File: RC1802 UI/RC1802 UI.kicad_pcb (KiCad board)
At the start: 2 copper layers, 99.1 x 80 mm, 47 parts, among them J1 Mount, J2 Mount, J3 Mount, J4 Mount, J6 CONN_02X20, SW1 CLEAR, SW10 IN5, SW11 IN6, SW12 IN7, SW2 IN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

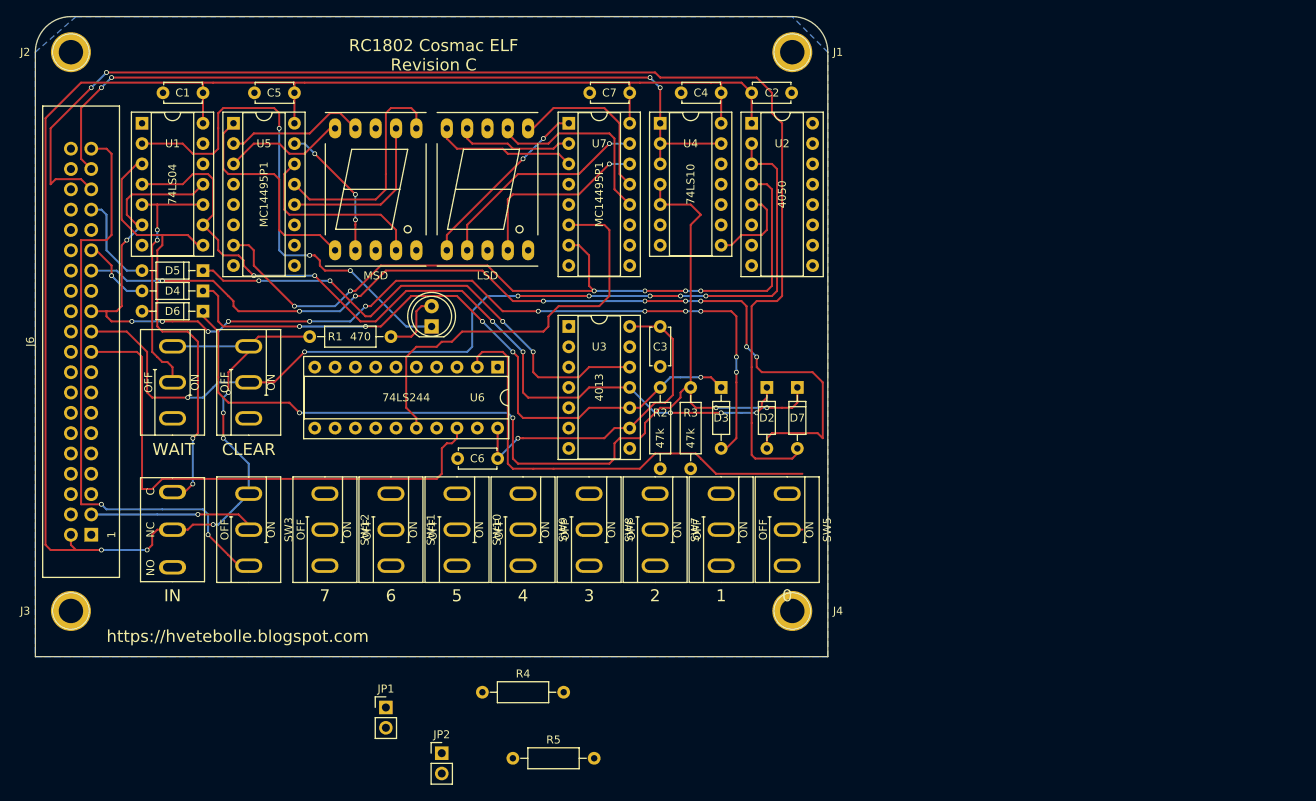
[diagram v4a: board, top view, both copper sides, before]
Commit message: Use proper switch names to ease use
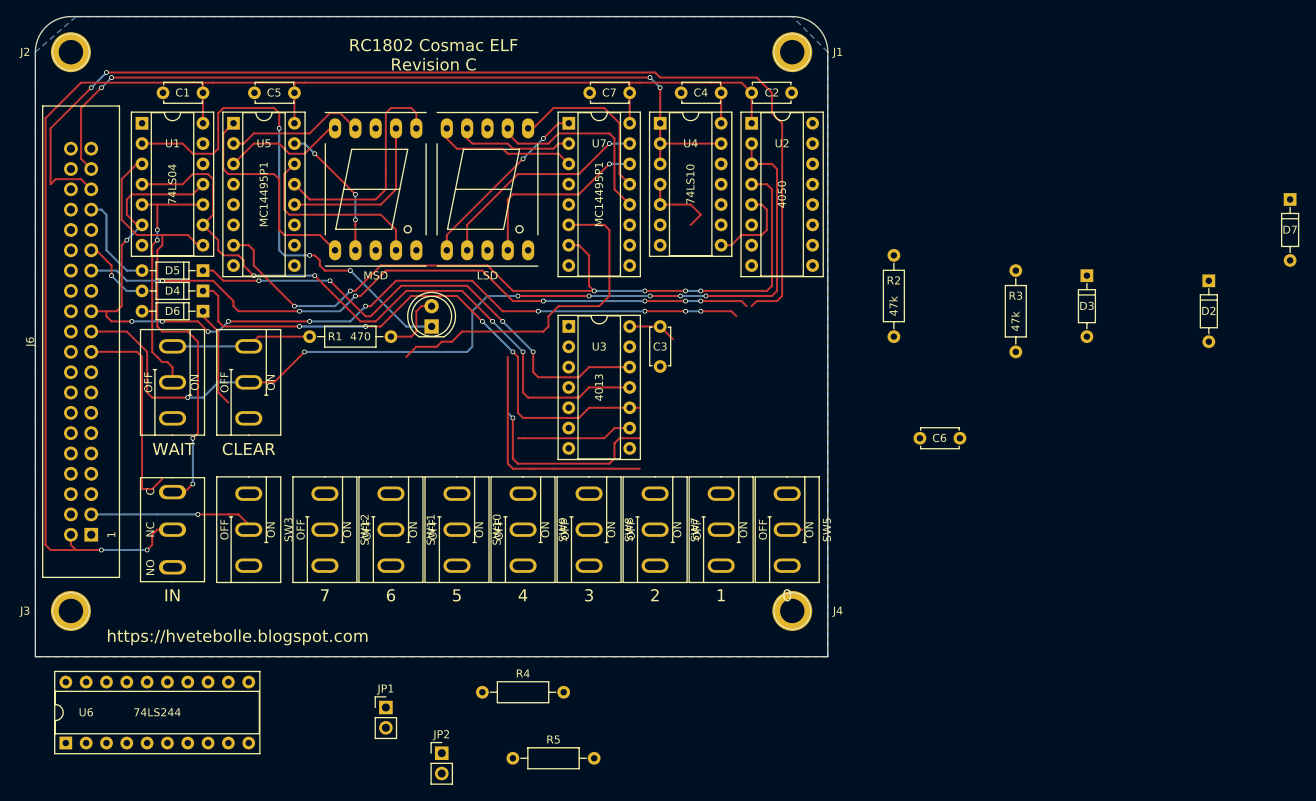
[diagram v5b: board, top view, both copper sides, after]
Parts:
- moved U6 71.6 mm to (104.1, 158.1), turned to 90 degrees
- moved D7 65.9 mm to (257.2, 90.2)
- moved C6 57.8 mm to (215.9, 120.0)
- moved D2 56.8 mm to (247.0, 100.3)
- moved D3 47.8 mm to (231.8, 99.7)
- moved R3 43.2 mm to (222.9, 109.2)
- moved R2 33.6 mm to (207.6, 107.3)
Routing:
- net VCC: track 338.4 -> 230.2 mm, vias 9 -> 2
- net LOAD_N2: track 131.4 -> 23.3 mm, vias 4 -> 0
- net Net-(SW5-Pad2): track 59.8 -> 1.91 mm
- net (no net): track 0.64 -> 55.3 mm, vias 0 -> 1
- net /BUS0: track 68.3 -> 26.2 mm
- net EF4: track 121.3 -> 88.3 mm, vias 9 -> 7
- net N2: track 162.6 -> 137.2 mm
- net /~IN: track 106.9 -> 86.0 mm, vias 7 -> 4
- net MWR: track 19.5 -> 0.06 mm
- net ~WAIT: track 132.2 -> 114.6 mm, vias 13 -> 11
- net Net-(D3-Pad1): track 83.7 -> 70.8 mm, vias 5 -> 4
- net /BUS1: track 52.3 -> 42.9 mm

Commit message: UI PCB layout incorporating changes
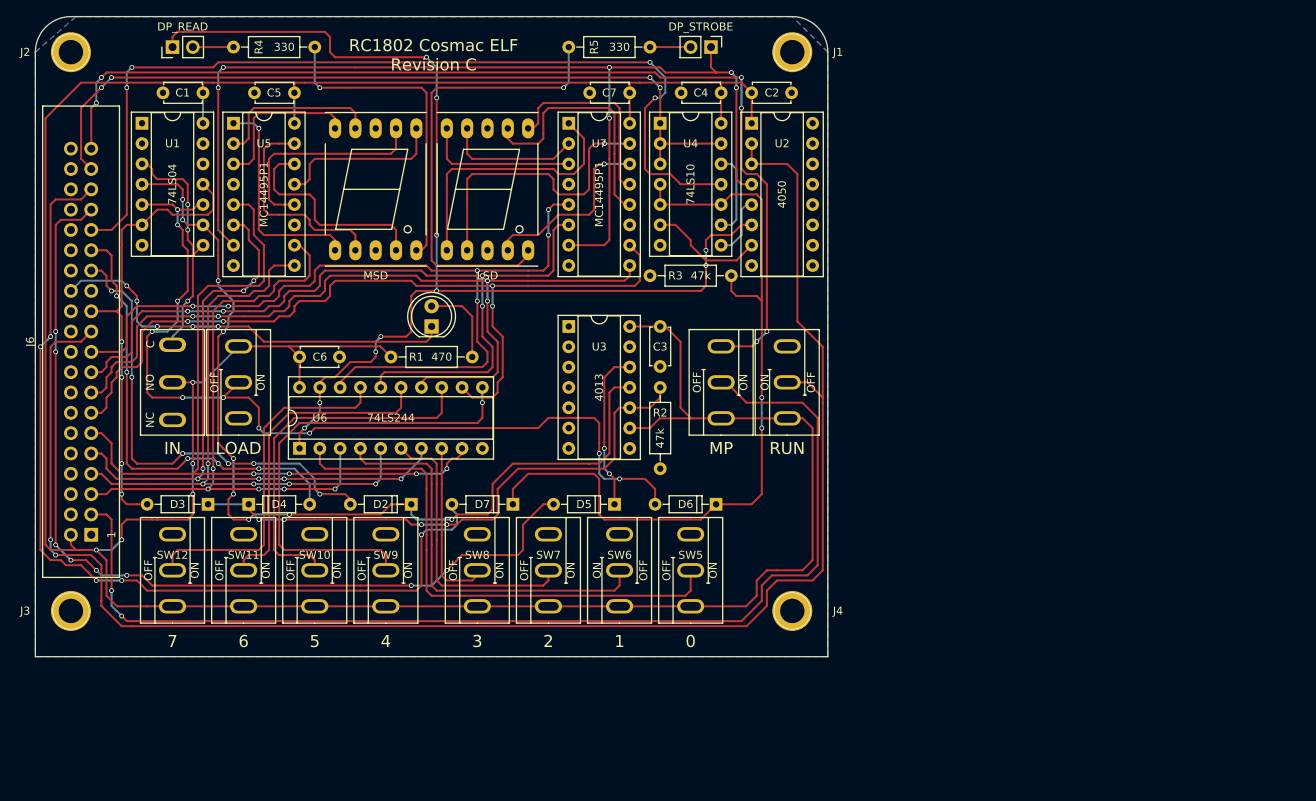
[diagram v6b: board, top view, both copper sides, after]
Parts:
- SW1: value CLEAR -> RUN
- SW4: value WAIT -> LOAD
- moved D3 113.5 mm to (121.9, 128.3), turned to 180 degrees
- moved D7 104.4 mm to (160.0, 128.3), turned to 180 degrees
- moved D2 103.5 mm to (147.3, 128.3), turned to 180 degrees
- moved JP2 94.5 mm to (184.8, 71.1), turned to 270 degrees
- moved R5 90.5 mm to (177.2, 71.1), turned to 180 degrees
- moved JP1 86.8 mm to (117.5, 71.1), turned to 90 degrees
- moved R4 86.4 mm to (125.1, 71.1)
- moved C6 83.2 mm to (133.3, 109.9), turned to 0 degrees
- moved D6 68.5 mm to (185.4, 128.3)
- moved SW1 67.3 mm to (194.3, 113.0), turned to 90 degrees
- moved SW3 61.9 mm to (186.1, 113.0)
- moved D5 59.2 mm to (172.7, 128.3)
- moved U6 47.0 mm to (133.3, 121.3)
- moved R3 46.7 mm to (177.2, 99.7), turned to 0 degrees
- moved R2 33.6 mm to (178.4, 123.8)
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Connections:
- J6 pad 10: GND -> (no net)
- J6 pad 12: GND -> (no net)
- J6 pad 14: GND -> (no net)
- J6 pad 16: GND -> (no net)
- J6 pad 18: GND -> (no net)
- J6 pad 20: GND -> (no net)
- J6 pad 22: GND -> (no net)
- J6 pad 24: GND -> (no net)
- J6 pad 28: GND -> (no net)
- J6 pad 30: GND -> (no net)
- J6 pad 32: GND -> (no net)
- J6 pad 34: GND -> (no net)
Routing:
- net VCC: track 230.2 -> 400.8 mm, vias 2 -> 5
- net READ: track 0.00 -> 144.0 mm, vias 0 -> 10
- net MWR: track 0.06 -> 130.2 mm, vias 0 -> 6
- net MP: track 20.8 -> 139.0 mm, vias 1 -> 2
- net TPB: track 0.00 -> 114.8 mm, vias 0 -> 4
- net /BUS3: track 0.00 -> 105.5 mm, vias 0 -> 4
- net DMA_IN: track 12.1 -> 115.6 mm, vias 0 -> 8
- net /BUS2: track 0.00 -> 102.3 mm, vias 0 -> 4
- net /BUS4: track 0.00 -> 95.8 mm, vias 0 -> 4
- net /BUS5: track 0.00 -> 84.9 mm, vias 0 -> 7
- net ~CLEAR: track 121.5 -> 203.6 mm, vias 7 -> 2
- net Net-(D6-Pad2): track 32.8 -> 114.6 mm, vias 2 -> 10
- net /BUS0: track 26.2 -> 107.3 mm, vias 0 -> 6
- net /BUS7: track 0.00 -> 77.8 mm, vias 0 -> 5
- net /BUS6: track 0.00 -> 77.3 mm, vias 0 -> 5
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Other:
- board text added: "LOAD"
- board text added: "MP"
- board text added: "RUN"
- board text removed: "CLEAR"
- board text removed: "WAIT"

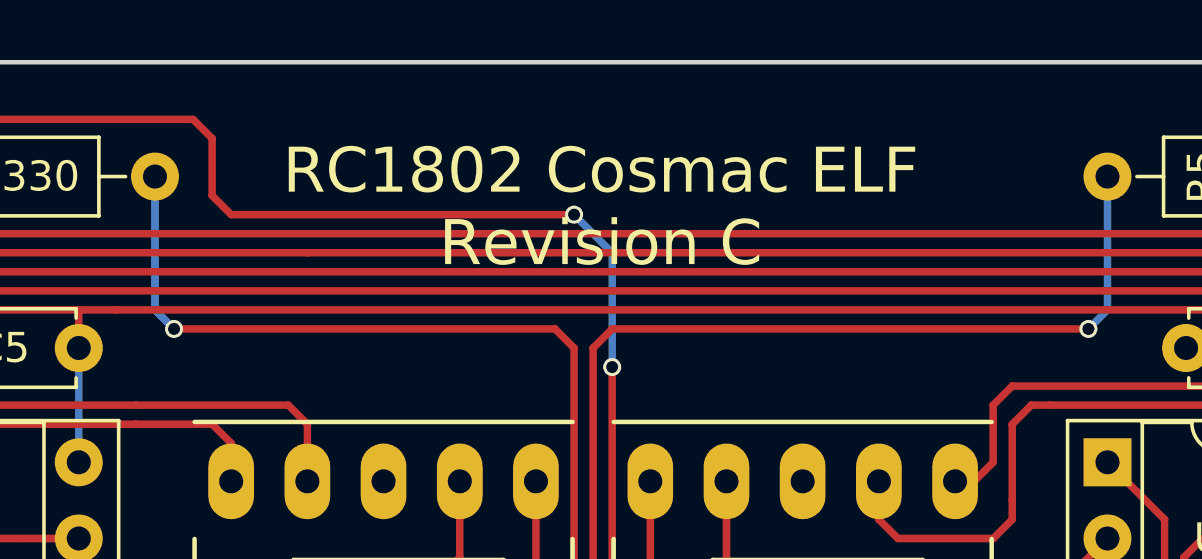
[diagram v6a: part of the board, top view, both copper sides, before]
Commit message: Gerber export UI board
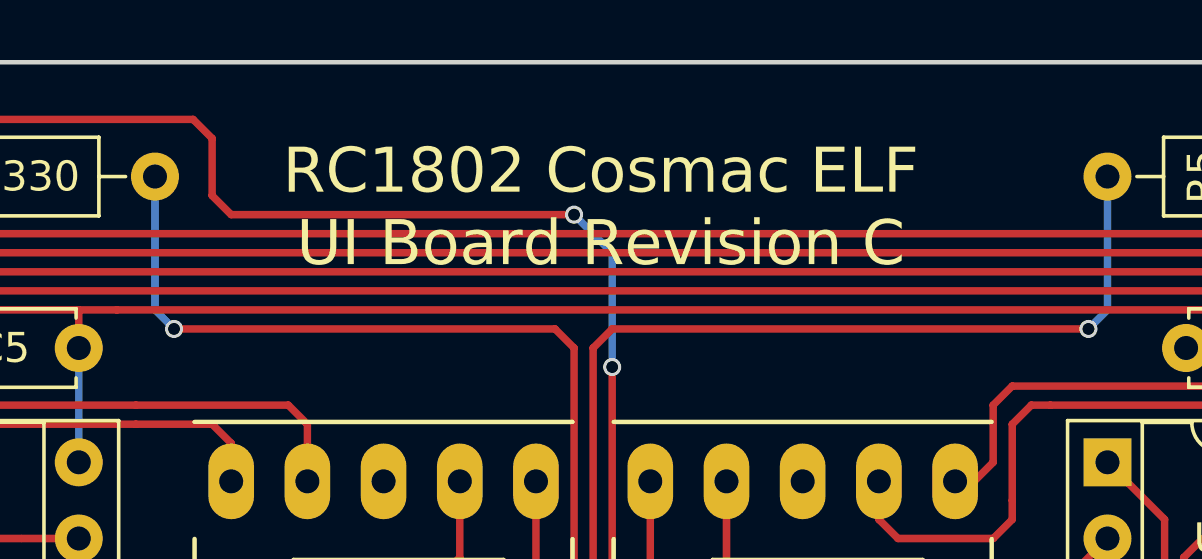
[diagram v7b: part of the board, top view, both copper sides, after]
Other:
- board text added: "RC1802 Cosmac ELF UI Board Revision C"
- board text removed: "RC1802 Cosmac ELF Revision C"
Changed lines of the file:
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@@
     (effects (font (size 1.5 1.5) (thickness 0.3)))
   )
-  (gr_text "RC1802 Cosmac ELF\nRevision C" (at 150.114 72.136) (layer F.SilkS)
+  (gr_text "RC1802 Cosmac ELF\nUI Board Revision C" (at 150.114 72.136) (layer F.SilkS)
     (effects (font (size 1.5 1.5) (thickness 0.3)))
   )

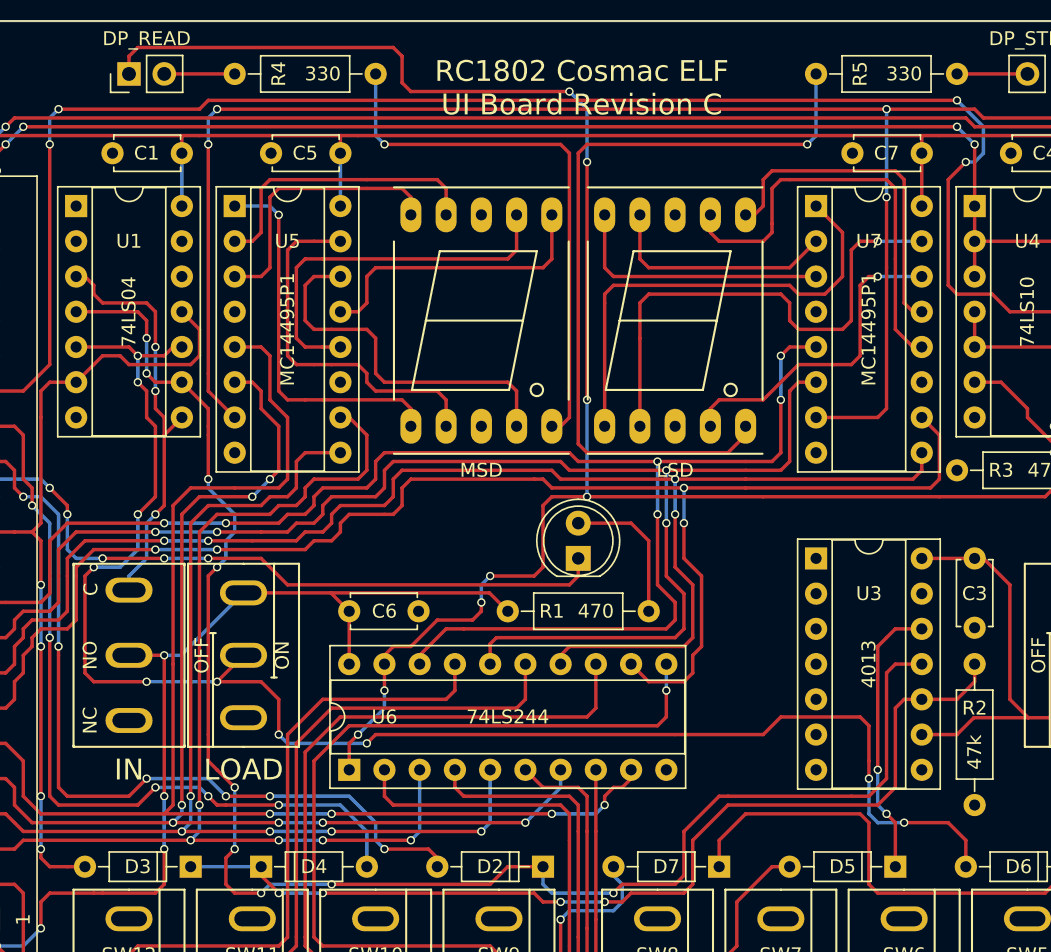
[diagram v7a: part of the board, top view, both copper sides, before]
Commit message: It all works, though LOAD was upside down...
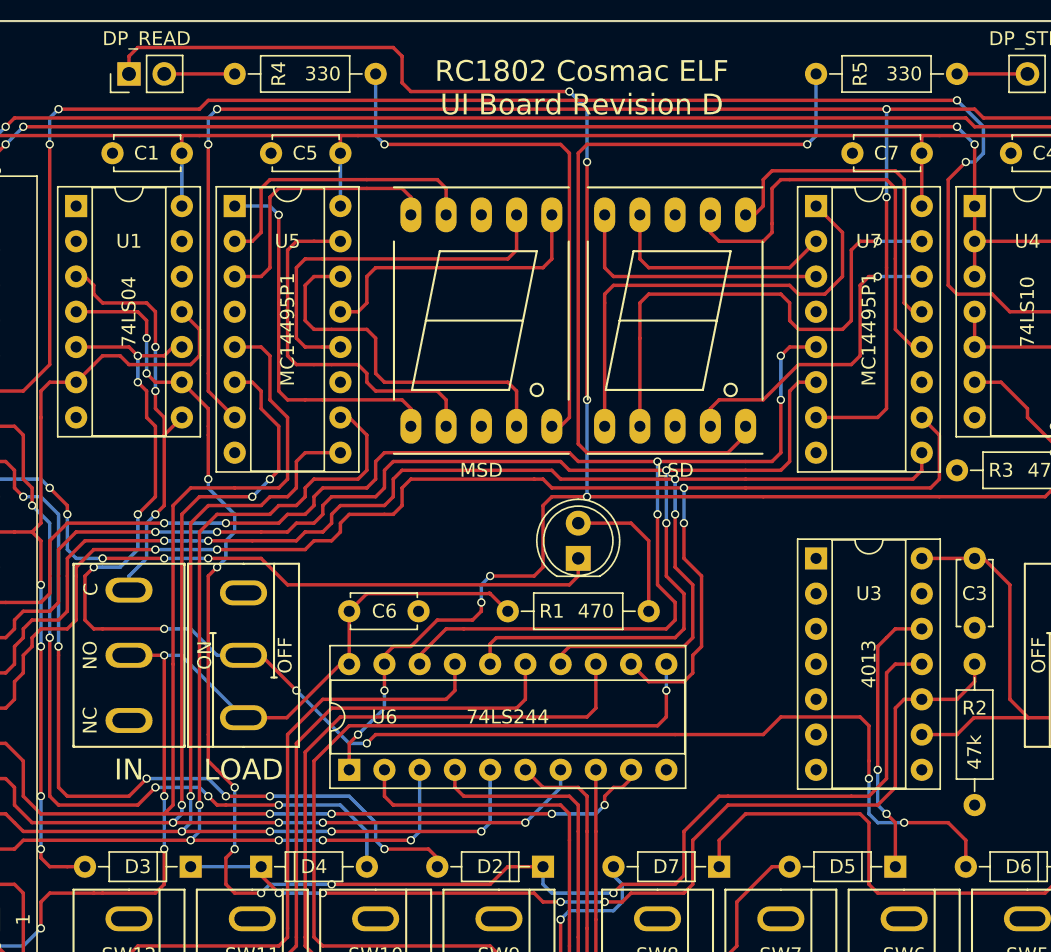
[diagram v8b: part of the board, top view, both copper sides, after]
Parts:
- turned SW4 to 90 degrees
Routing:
- net Net-(D6-Pad2): track 114.6 -> 108.2 mm, vias 10 -> 9
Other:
- board text added: "RC1802 Cosmac ELF UI Board Revision D"
- board text removed: "RC1802 Cosmac ELF UI Board Revision C"
